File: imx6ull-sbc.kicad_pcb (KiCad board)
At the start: 4 copper layers, 142 parts, among them J1 Micro_SD_Card_Det1, P1 USB_C_Plug_USB2.0, SW1 CAS-220TA, U1 MX6UL-VM, U2 MC32PF1510A6EP, U3 MT41K256M16, U4 TUSB320, U5 FPF2498BUCX, U6 TPD4EUSB30, U7 D5V0H1B2LP, U8 D5V0H1B2LP, U9 W25Q32JVZP, Y1 24Mhz, Y2 32.768kHz

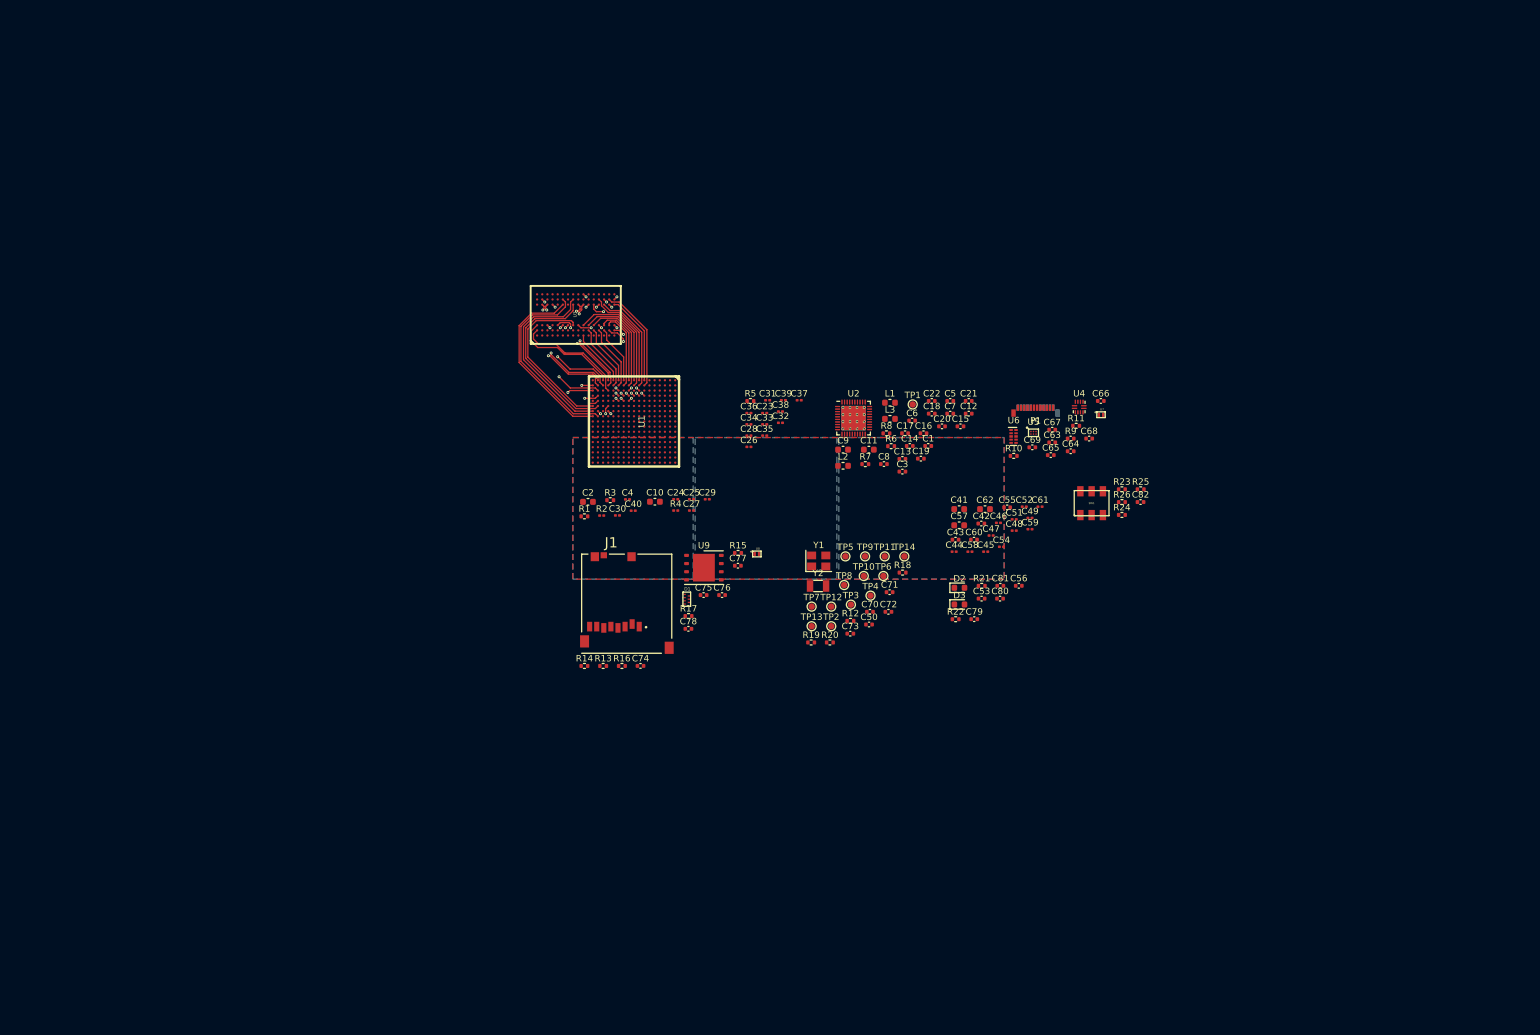
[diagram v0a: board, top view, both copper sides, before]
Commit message: more ddr routing, add more connectors
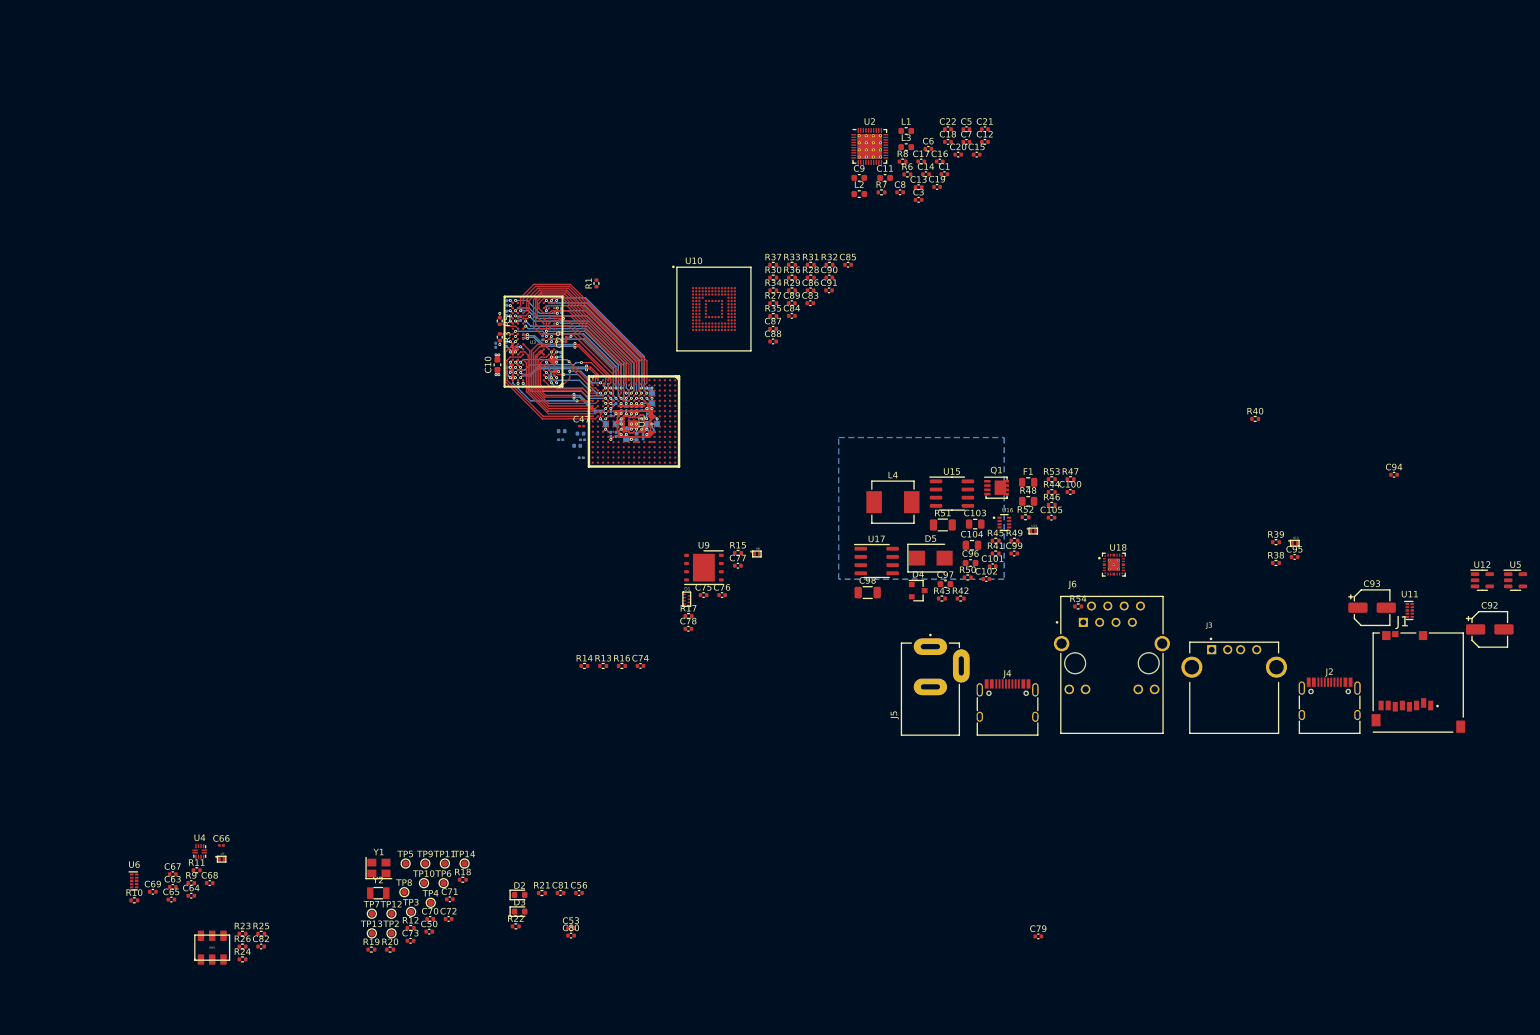
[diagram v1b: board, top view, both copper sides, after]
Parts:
- removed P1: USB_C_Plug_USB2.0, Connector_USB:USB_C_Plug_Molex_105444
- removed TP1: TestPoint, TestPoint:TestPoint_Pad_D1.0mm
- added C100: 68pF, Capacitor_SMD:C_0402_1005Metric, F.Cu at (172.3, 87.5)
- added C101: 15nF, Capacitor_SMD:C_0402_1005Metric, F.Cu at (160.2, 99.0)
- added C102: 0.1uF, Capacitor_SMD:C_0402_1005Metric, F.Cu at (159.2, 101.0)
- added C103: 22uF, Capacitor_SMD:C_0805_2012Metric, F.Cu at (157.5, 92.4)
- added C104: 22uF, Capacitor_SMD:C_0805_2012Metric, F.Cu at (157.0, 95.7)
- added C105: 0.1uF, Capacitor_SMD:C_0402_1005Metric, F.Cu at (169.3, 91.4)
- added C83: 0.1uF, Capacitor_SMD:C_0402_1005Metric, F.Cu at (131.9, 58.1)
- added C84: 4.7uF, Capacitor_SMD:C_0402_1005Metric, F.Cu at (129.0, 60.1)
- added C85: 0.1uF, Capacitor_SMD:C_0402_1005Metric, F.Cu at (137.8, 52.2)
- added C86: 0.1uF, Capacitor_SMD:C_0402_1005Metric, F.Cu at (131.9, 56.1)
- added C87: 0.1uF, Capacitor_SMD:C_0402_1005Metric, F.Cu at (126.1, 62.1)
- added C88: 0.1uF, Capacitor_SMD:C_0402_1005Metric, F.Cu at (126.1, 64.1)
- added C89: 0.1uF, Capacitor_SMD:C_0402_1005Metric, F.Cu at (129.0, 58.1)
- added C90: 4.7uF, Capacitor_SMD:C_0402_1005Metric, F.Cu at (134.8, 54.1)
- added C91: 4.7uF, Capacitor_SMD:C_0402_1005Metric, F.Cu at (134.8, 56.1)
- added C92: 120uF, Capacitor_SMD:CP_Elec_5x5.8, F.Cu at (237.4, 108.8)
- added C93: 120uF, Capacitor_SMD:CP_Elec_5x5.8, F.Cu at (219.2, 105.4)
- added C94: 0.1uF, Capacitor_SMD:C_0402_1005Metric, F.Cu at (222.6, 84.8)
- added C95: 0.1uF, Capacitor_SMD:C_0402_1005Metric, F.Cu at (207.1, 97.5)
- added C96: 0.1uF, Capacitor_SMD:C_0603_1608Metric, F.Cu at (156.8, 98.5)
- added C97: 0.1uF, Capacitor_SMD:C_0603_1608Metric, F.Cu at (152.9, 101.8)
- added C98: 10uF, Capacitor_SMD:C_1206_3216Metric, F.Cu at (140.8, 103.1)
- added C99: 1800pF, Capacitor_SMD:C_0402_1005Metric, F.Cu at (163.6, 97.0)
- added D4: BZX84Cxx, Diode_SMD:D_SOT-23_ANK, F.Cu at (148.7, 102.8)
- added D5: B230, Diode_SMD:D_SMB, F.Cu at (150.6, 97.7)
- added F1: Fuse, Fuse:Fuse_0805_2012Metric, F.Cu at (165.7, 86.0)
- added J2: USB4105, Connector_USB:USB_C_Receptacle_HRO_TYPE-C-31-M-12, F.Cu at (212.6, 121.0)
- added J3: USB1130, imx6ull-sbc:GCT_USB1130-15-A_REVA, F.Cu at (197.7, 114.7)
- added J4: USB4105, Connector_USB:USB_C_Receptacle_HRO_TYPE-C-31-M-12, F.Cu at (162.5, 121.3)
- added J5: Barrel_Jack_Switch, imx6ull-sbc:TENSILITY_54-00167, F.Cu at (150.5, 125.2)
- added J6: CRJ011-ML3-TH, imx6ull-sbc:CUI_CRJ011-ML3-TH, F.Cu at (178.7, 114.1)
- added L4: 22uH, Inductor_SMD:L_Vishay_IHLP-2525, F.Cu at (144.7, 89.0)
- added Q1: SiSA35DN, Package_SO:Vishay_PowerPAK_1212-8_Single, F.Cu at (160.8, 86.8)
- added R27: 10R, Resistor_SMD:R_0402_1005Metric, F.Cu at (126.1, 58.1)
- added R28: 10K, Resistor_SMD:R_0402_1005Metric, F.Cu at (131.9, 54.2)
- added R29: 10K, Resistor_SMD:R_0402_1005Metric, F.Cu at (129.0, 56.1)
- added R30: 10K, Resistor_SMD:R_0402_1005Metric, F.Cu at (126.1, 54.2)
- added R31: 10K, Resistor_SMD:R_0402_1005Metric, F.Cu at (131.9, 52.2)
- added R32: 10K, Resistor_SMD:R_0402_1005Metric, F.Cu at (134.9, 52.2)
- added R33: 10K, Resistor_SMD:R_0402_1005Metric, F.Cu at (129.0, 52.2)
- added R34: 10K, Resistor_SMD:R_0402_1005Metric, F.Cu at (126.1, 56.1)
- added R35: 10K, Resistor_SMD:R_0402_1005Metric, F.Cu at (126.1, 60.1)
- added R36: 10K, Resistor_SMD:R_0402_1005Metric, F.Cu at (129.0, 54.2)
- added R37: 10K, Resistor_SMD:R_0402_1005Metric, F.Cu at (126.1, 52.2)
- added R38: 10K, Resistor_SMD:R_0402_1005Metric, F.Cu at (204.2, 98.5)
- added R39: 10K, Resistor_SMD:R_0402_1005Metric, F.Cu at (204.2, 95.3)
- added R40: 0R, Resistor_SMD:R_0402_1005Metric, F.Cu at (201.0, 76.1)
- added R41: 5.1K, Resistor_SMD:R_0402_1005Metric, F.Cu at (160.7, 97.0)
- added R42: 100K, Resistor_SMD:R_0402_1005Metric, F.Cu at (155.2, 104.0)
- added R43: 5.1K, Resistor_SMD:R_0402_1005Metric, F.Cu at (152.3, 104.0)
- added R44: 21K, Resistor_SMD:R_0402_1005Metric, F.Cu at (169.4, 87.5)
- added R45: 0R, Resistor_SMD:R_0402_1005Metric, F.Cu at (160.7, 95.0)
- added R46: 0R, Resistor_SMD:R_0402_1005Metric, F.Cu at (169.4, 89.5)
- added R47: 10K, Resistor_SMD:R_0402_1005Metric, F.Cu at (172.3, 85.5)
- added R48: 0R, Resistor_SMD:R_0805_2012Metric, F.Cu at (165.7, 88.9)
- added R49: 10K, Resistor_SMD:R_0402_1005Metric, F.Cu at (163.6, 95.0)
- added R50: 1.91K, Resistor_SMD:R_0402_1005Metric, F.Cu at (156.3, 100.7)
- added R51: 0.1R, Resistor_SMD:R_1206_3216Metric, F.Cu at (152.5, 92.6)
- added R52: 10K, Resistor_SMD:R_0402_1005Metric, F.Cu at (165.3, 91.4)
- added R53: 10K, Resistor_SMD:R_0402_1005Metric, F.Cu at (169.4, 85.5)
- added R54: 10K, Resistor_SMD:R_0402_1005Metric, F.Cu at (173.5, 105.2)
- added U10: SFEM064GB1ED1TO-I-6F-111-STD, imx6ull-sbc:BGA153N50P14X14_1150X1300X100, F.Cu at (116.9, 59.0)
- added U11: TPD4EUSB30, Package_SON:USON-10_2.5x1.0mm_P0.5mm, F.Cu at (225.0, 105.9)
- added U12: 74LVC1G06, Package_TO_SOT_SMD:SOT-23-5, F.Cu at (236.3, 101.2)
- added U13: D5V0H1B2LP, imx6ull-sbc:DFN100X60X45-2N, F.Cu at (207.2, 95.4)
- added U14: D5V0H1B2LP, imx6ull-sbc:DFN100X60X45-2N, F.Cu at (166.5, 93.5)
- added U15: TPS54233, Package_SO:SOIC-8_3.9x4.9mm_P1.27mm, F.Cu at (153.9, 87.7)
- added U16: TPS2116DRLR, imx6ull-sbc:SOTFL50P160X60-8N, F.Cu at (162.0, 92.2)
- added U17: INA219BxD, Package_SO:SOIC-8_3.9x4.9mm_P1.27mm, F.Cu at (142.2, 98.2)
- added U18: DP83825IRMQR, imx6ull-sbc:XCVR_DP83825IRMQR, F.Cu at (179.0, 98.7)
- C2, C23, C24, C25, C26, C27, C28, C30, C31, C32, C33, C34, C35, C36, C37, C38, C39, C4, C40, C41, C42, C43, C44, C45, C46, C48, C49, C51, C52, C54, C55, C57, C58, C59, C60, C61, C62, R2, R4: moved to B.Cu
- C66: footprint Capacitor_SMD:C_0402_1005Metric -> Capacitor_SMD:C_0201_0603Metric
- C67: value 4.7uF -> 0.1uF
- C69: value 4.7uF -> 1uF
- U5: value FPF2498BUCX -> AP22814AW5; footprint Package_CSP:WLCSP-6_1.4x1.0mm_P0.4mm -> Package_TO_SOT_SMD:SOT-23-5
- moved C63 153.1 mm to (32.9, 148.8)
- moved C64 153.1 mm to (35.7, 150.2)
- moved C65 153.1 mm to (32.6, 150.8)
- moved C66 153.1 mm to (40.4, 142.4)
- moved C67 153.1 mm to (32.9, 146.8)
- moved C82 153.1 mm to (46.6, 158.1)
- moved R11 153.1 mm to (36.6, 146.2)
- moved R9 153.1 mm to (35.7, 148.2)
- moved SW1 153.1 mm to (39.0, 158.2)
- moved U4 153.1 mm to (37.0, 143.3)
- moved U6 153.1 mm to (26.9, 147.9)
- moved U7 153.1 mm to (40.5, 144.5)
- moved C68 153.1 mm to (38.6, 148.2)
- moved C69 153.1 mm to (29.8, 149.6)
- moved R10 153.1 mm to (26.9, 150.9)
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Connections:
- C13 pad 1: Net-(C13-Pad1) -> EMMC_1V8
- C67 pad 1: /USB/USB_VBUS -> /USB/VBUS_1
- C74 pad 1: DCDC_3V3 -> EMMC_1V8
- R9 pad 1: /USB/USB_VBUS -> /USB/VBUS_1
- U1 pad A5: unconnected-(U1-PadA5) -> /Storage/SD2_DATA7
- U1 pad A6: unconnected-(U1-PadA6) -> /Storage/SD2_DATA6
- U1 pad A7: unconnected-(U1-PadA7) -> /Storage/SD2_DATA2
- U1 pad B4: unconnected-(U1-PadB4) -> /Storage/SD2_nRST
- U1 pad B6: unconnected-(U1-PadB6) -> /Storage/SD2_DATA5
- U1 pad B7: unconnected-(U1-PadB7) -> /Storage/SD2_DATA1
- U1 pad C6: unconnected-(U1-PadC6) -> /Storage/SD2_DATA4
- U1 pad C8: unconnected-(U1-PadC8) -> /Storage/SD2_CMD
- U1 pad D6: unconnected-(U1-PadD6) -> /Storage/SD2_DATA3
- U1 pad D7: unconnected-(U1-PadD7) -> /Storage/SD2_DATA0
- U1 pad D8: unconnected-(U1-PadD8) -> /Storage/SD2_CLK_R
- U1 pad E7: DCDC_3V3 -> EMMC_1V8
- U1 pad F15: PMIC_WDI -> unconnected-(U1-PadF15)
- U1 pad M15: unconnected-(U1-PadM15) -> PMIC_WDI
- U1 pad T13: unconnected-(U1-PadT13) -> /USB/USB2D_N
- U1 pad T15: /USB/USBD_N -> /USB/USB1D_N
- U1 pad U13: unconnected-(U1-PadU13) -> /USB/USB2D_P
- U1 pad U15: /USB/USBD_P -> /USB/USB1D_P
- U2 pad 29: Net-(C13-Pad1) -> EMMC_1V8
- U3 pad F8: /DDR/DRAM_D5 -> /DDR/DRAM_D3
- U3 pad H8: /DDR/DRAM_D3 -> /DDR/DRAM_D5
- U4 pad 2: unconnected-(U4-Pad2) -> /USB/CC2
- U4 pad 9: unconnected-(U4-Pad9) -> USB1_ID
- U7 pad 1: /USB/USB_VBUS -> /USB/VBUS_1
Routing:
- net GND: track 0.00 -> 134.2 mm, vias 0 -> 51
- net DDR_1V35: track 0.00 -> 44.6 mm, vias 0 -> 25
- net /IMX6ULL Power/VDD_SOC_CAP: track 0.00 -> 21.7 mm, vias 0 -> 5
- net VDD_ARM_SOC_IN: track 0.00 -> 21.7 mm, vias 0 -> 4
- net /DDR/DRAM_D6: track 1.35 -> 19.6 mm
- net /DDR/DRAM_D10: track 0.00 -> 16.7 mm, vias 0 -> 2
- net /DDR/DRAM_D7: track 0.00 -> 15.1 mm
- net /DDR/DRAM_D12: track 0.00 -> 14.8 mm, vias 0 -> 2
- net /DDR/DRAM_A6: track 16.6 -> 31.2 mm
- net /DDR/DRAM_A14: track 14.0 -> 28.0 mm
- net /DDR/DRAM_A1: track 16.0 -> 29.6 mm
- net /DDR/DRAM_SDBA1: track 16.1 -> 29.1 mm
- net /DDR/DRAM_CAS_B: track 18.5 -> 31.0 mm
- net /DDR/DRAM_A13: track 11.9 -> 24.4 mm
- net /DDR/DRAM_RESET_B: track 12.8 -> 25.3 mm
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- added copper zone on In1.Cu, net DCDC_3V3
- added copper zone on In2.Cu, net DDR_1V35
- removed copper zone on B.Cu, net DDR_1V35
- removed copper zone on F.Cu, net GND
- removed copper zone on In1.Cu, net GND
